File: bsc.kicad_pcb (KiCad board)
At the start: 2 copper layers, 120 x 72 mm, 155 parts, among them IC1 ILD217T, IC2 ILD217T, J1 AVR-ISP-6, J2 Prog, J3 U0TXD silent, J4 Boot, K1 TIANBO-HJR-4102-L, K2 TIANBO-HJR-4102-L, K3 TIANBO-HJR-4102-L, K4 TIANBO-HJR-4102-L, K5 TIANBO-HJR-4102-L, K6 TIANBO-HJR-4102-L, K7 TIANBO-HJR-4102-L, K8 AQY210S, Q1 BSS138, Q10 BC846, Q11 BC846, Q2 BSS138, Q3 BSS138, Q4 BSS138, Q5 BSS138, Q6 BSS138, Q7 BSS138, Q8 BC846, Q9 BC846, U1 LMO78_03-0.5, U10 74HC595, U11 74HC14, U12 74HC165, U2 ESP32WROOM32E16, U3 ATtiny24A-SS, U4 ADuM1201AR, U5 ADuM1201AR, U6 ADuM1201AR, U7 SN65HVD234, U8 SP3485EN, U9 SP3485EN, X1 Conn_S2, X2 Conn_S1, X3 Conn_DI, X4 Conn_SV, X5 Conn_Rel2, X6 Conn_Rel1

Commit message: Redesign PCB
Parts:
- removed J3: U0TXD silent, Connector_PinHeader_2.54mm:PinHeader_1x02_P2.54mm_Vertical
- removed K1: TIANBO-HJR-4102-L, Relay_THT:Relay_SPDT_HJR-4102
- removed K8: AQY210S, SamacSys_Parts:SOP254P962X275-4N
- removed R9: 180R, Resistor_SMD:R_0603_1608Metric
- removed U3: ATtiny24A-SS, Package_SO:SOIC-14_3.9x8.7mm_P1.27mm
- added C29: 22µ, Capacitor_SMD:CP_Elec_4x5.8, F.Cu at (115.6, 59.7)
- added C30: 100n, Capacitor_SMD:C_0603_1608Metric, F.Cu at (82.2, 49.7)
- added C31: 100n, Capacitor_SMD:C_0603_1608Metric, F.Cu at (107.4, 52.2)
- added C32: 100n, Capacitor_SMD:C_0603_1608Metric, F.Cu at (82.2, 42.2)
- added C33: 100n, Capacitor_SMD:C_0603_1608Metric, F.Cu at (107.4, 44.1)
- added C34: 22µ, Capacitor_SMD:CP_Elec_4x5.8, F.Cu at (85.1, 45.5)
- added C35: 22µ, Capacitor_SMD:CP_Elec_4x5.8, F.Cu at (109.5, 48.0)
- added C36: 100n, Capacitor_SMD:C_0603_1608Metric, B.Cu at (69.6, 49.0)
- added C37: 100n, Capacitor_SMD:C_0603_1608Metric, B.Cu at (94.9, 49.0)
- added C38: 100n, Capacitor_SMD:C_0603_1608Metric, F.Cu at (94.9, 49.7)
- added C39: 100n, Capacitor_SMD:C_0603_1608Metric, F.Cu at (94.9, 42.1)
- added C40: 100n, Capacitor_SMD:C_0603_1608Metric, F.Cu at (72.8, 50.2)
- added C41: 100n, Capacitor_SMD:C_0603_1608Metric, F.Cu at (84.8, 50.7)
- added C42: 22µ, Capacitor_SMD:CP_Elec_4x5.8, F.Cu at (97.8, 45.5)
- added C43: 100n, Capacitor_SMD:C_0603_1608Metric, F.Cu at (97.4, 49.9)
- added C44: 100n, Capacitor_SMD:C_0603_1608Metric, F.Cu at (74.0, 62.1)
- added C45: 100n, Capacitor_SMD:C_0603_1608Metric, B.Cu at (82.2, 49.0)
- added C46: 100n, Capacitor_SMD:C_0603_1608Metric, F.Cu at (88.1, 66.2)
- added C47: 100n, Capacitor_SMD:C_0603_1608Metric, F.Cu at (102.9, 63.5)
- added C48: 100n, Capacitor_SMD:C_0603_1608Metric, B.Cu at (42.5, 66.3)
- added C49: 100n, Capacitor_SMD:C_0603_1608Metric, F.Cu at (61.6, 78.0)
- added C50: 100µ, Capacitor_SMD:CP_Elec_6.3x5.9, F.Cu at (53.3, 87.7)
- added C51: 100n, Capacitor_SMD:C_0603_1608Metric, F.Cu at (65.5, 88.3)
- added C52: 100µ, Capacitor_SMD:CP_Elec_6.3x5.9, F.Cu at (52.6, 80.4)
- added C53: 100n, Capacitor_SMD:C_0603_1608Metric, F.Cu at (62.3, 88.4)
- added C54: 100n, Capacitor_SMD:C_0603_1608Metric, B.Cu at (41.0, 66.3)
- added C55: 100n, Capacitor_SMD:C_0603_1608Metric, B.Cu at (44.2, 66.3)
- added C60: 100n, Capacitor_SMD:C_0603_1608Metric, F.Cu at (73.0, 80.8)
- added D24: LL4148, Diode_SMD:D_MiniMELF, B.Cu at (72.1, 36.8)
- added F1: BELFUSE, Fuse:Fuse_0679H, F.Cu at (36.0, 89.1)
- added F2: BELFUSE, Fuse:Fuse_0679H, F.Cu at (44.1, 89.1)
- added H1: MountingHole, MountingHole:MountingHole_3.2mm_M3, F.Cu at (35.0, 21.0)
- added H2: MountingHole, MountingHole:MountingHole_3.2mm_M3, F.Cu at (145.0, 21.0)
- added H3: MountingHole, MountingHole:MountingHole_3.2mm_M3, F.Cu at (145.0, 111.0)
- added H4: MountingHole, MountingHole:MountingHole_3.2mm_M3, F.Cu at (35.0, 111.0)
- added IC3: ILD217T, Package_SO:SOIC-8_5.23x5.23mm_P1.27mm, F.Cu at (67.7, 58.4)
- added IC4: ILD217T, Package_SO:SOIC-8_5.23x5.23mm_P1.27mm, F.Cu at (88.6, 58.4)
- added J10: JP_REL1_COM_12V, Connector_PinHeader_2.54mm:PinHeader_1x02_P2.54mm_Vertical, F.Cu at (137.9, 89.2)
- added J11: Conn_Extension, Connector_PinHeader_2.54mm:PinHeader_2x05_P2.54mm_Vertical, F.Cu at (33.1, 74.5)
- added J12: JP_REL2_COM_12V, Connector_PinHeader_2.54mm:PinHeader_1x02_P2.54mm_Vertical, F.Cu at (125.2, 89.2)
- added J13: JP_REL3_COM_12V, Connector_PinHeader_2.54mm:PinHeader_1x02_P2.54mm_Vertical, F.Cu at (112.5, 89.2)
- added J14: Conn_REL1, Connector_PinHeader_2.54mm:PinHeader_1x03_P2.54mm_Vertical, F.Cu at (135.1, 75.7)
- added J15: Conn_REL2, Connector_PinHeader_2.54mm:PinHeader_1x03_P2.54mm_Vertical, F.Cu at (135.1, 85.1)
- added J16: Conn_REL3, Connector_PinHeader_2.54mm:PinHeader_1x03_P2.54mm_Vertical, F.Cu at (108.7, 80.5)
- added J5: JP_REL4_COM_12V, Connector_PinHeader_2.54mm:PinHeader_1x02_P2.54mm_Vertical, F.Cu at (99.8, 89.2)
- added J8: JP_REL5_COM_12V, Connector_PinHeader_2.54mm:PinHeader_1x02_P2.54mm_Vertical, F.Cu at (87.1, 89.2)
- added J9: JP_REL6_COM_12V, Connector_PinHeader_2.54mm:PinHeader_1x02_P2.54mm_Vertical, F.Cu at (74.4, 89.2)
- added JP10: JP_U1_TX_TXS, Jumper:SolderJumper-2_P1.3mm_Open_RoundedPad1.0x1.5mm, B.Cu at (71.1, 62.7)
- added JP11: JP_U1_RXS_RXO, Jumper:SolderJumper-2_P1.3mm_Open_RoundedPad1.0x1.5mm, B.Cu at (76.5, 54.5)
- added JP12: JP_U1_TXS_TXO, Jumper:SolderJumper-2_P1.3mm_Open_RoundedPad1.0x1.5mm, B.Cu at (68.6, 54.5)
- added JP13: JP_U1_TXEN_TXENS, Jumper:SolderJumper-2_P1.3mm_Open_RoundedPad1.0x1.5mm, F.Cu at (67.1, 57.1)
- added JP14: JP_U2_3V3_VCC, Jumper:SolderJumper-2_P1.3mm_Open_RoundedPad1.0x1.5mm, B.Cu at (93.0, 40.6)
- added JP15: JP_U2_GND_GNDS, Jumper:SolderJumper-2_P1.3mm_Open_RoundedPad1.0x1.5mm, B.Cu at (89.4, 51.3)
- added JP16: JP_U2_RX_RXS, Jumper:SolderJumper-2_P1.3mm_Open_RoundedPad1.0x1.5mm, B.Cu at (91.7, 62.7)
- added JP17: JP_U2_TX_TXS, Jumper:SolderJumper-2_P1.3mm_Open_RoundedPad1.0x1.5mm, B.Cu at (83.6, 62.7)
- added JP18: JP_U2_RXS_RXO, Jumper:SolderJumper-2_P1.3mm_Open_RoundedPad1.0x1.5mm, B.Cu at (88.9, 54.5)
- added JP19: JP_U2_TXS_TXO, Jumper:SolderJumper-2_P1.3mm_Open_RoundedPad1.0x1.5mm, B.Cu at (81.0, 54.5)
- added JP20: JP_U2_TXEN_TXENS, Jumper:SolderJumper-2_P1.3mm_Open_RoundedPad1.0x1.5mm, F.Cu at (67.1, 59.7)
- added JP21: JP_U3_3V3_VCC, Jumper:SolderJumper-2_P1.3mm_Open_RoundedPad1.0x1.5mm, B.Cu at (105.8, 40.6)
- added JP22: JP_U3_GND_GNDS, Jumper:SolderJumper-2_P1.3mm_Open_RoundedPad1.0x1.5mm, B.Cu at (102.1, 51.6)
- added JP23: JP_U3_RX_RXS, Jumper:SolderJumper-2_P1.3mm_Open_RoundedPad1.0x1.5mm, B.Cu at (101.2, 62.4)
- added JP24: JP_U3_TX_TXS, Jumper:SolderJumper-2_P1.3mm_Open_RoundedPad1.0x1.5mm, B.Cu at (98.7, 62.4)
- added JP25: JP_U3_RXS_RXO, Jumper:SolderJumper-2_P1.3mm_Open_RoundedPad1.0x1.5mm, B.Cu at (101.1, 54.7)
- added JP26: JP_U3_TXS_TXO, Jumper:SolderJumper-2_P1.3mm_Open_RoundedPad1.0x1.5mm, B.Cu at (93.2, 54.7)
- added JP27: JP_U3_TXEN_TXENS, Jumper:SolderJumper-2_P1.3mm_Open_RoundedPad1.0x1.5mm, F.Cu at (87.4, 57.7)
- added JP28: 12V_5V, Jumper:SolderJumper-2_P1.3mm_Open_RoundedPad1.0x1.5mm, B.Cu at (59.6, 82.3)
- added JP29: JP_REL_VCC, Jumper:SolderJumper-3_P1.3mm_Open_RoundedPad1.0x1.5mm, B.Cu at (56.5, 91.4)
- added JP30: JP_EXT_5V, Jumper:SolderJumper-2_P1.3mm_Open_RoundedPad1.0x1.5mm, B.Cu at (36.4, 87.4)
- added JP31: JP_EXT_3V3, Jumper:SolderJumper-2_P1.3mm_Open_RoundedPad1.0x1.5mm, B.Cu at (38.1, 81.5)
- added JP7: JP_U1_3V3_VCC, Jumper:SolderJumper-2_P1.3mm_Open_RoundedPad1.0x1.5mm, B.Cu at (80.4, 40.6)
- added JP8: JP_U1_GND_GNDS, Jumper:SolderJumper-2_P1.3mm_Open_RoundedPad1.0x1.5mm, B.Cu at (76.6, 51.3)
- added JP9: JP_U1_RX_RXS, Jumper:SolderJumper-2_P1.3mm_Open_RoundedPad1.0x1.5mm, B.Cu at (79.0, 62.7)
- added PS1: 1S4E_0503S1U, custom_th:Converter_DCDC_GAPTEC_1S4E_S1U, F.Cu at (66.9, 50.9)
- added PS2: TEA 1-0505, Converter_DCDC:Converter_DCDC_Murata_MEE1SxxxxSC_THT, F.Cu at (111.6, 65.6)
- added PS3: 1S4E_0503S1U, custom_th:Converter_DCDC_GAPTEC_1S4E_S1U, F.Cu at (79.4, 50.8)
- added PS4: 1S4E_0503S1U, custom_th:Converter_DCDC_GAPTEC_1S4E_S1U, F.Cu at (104.8, 50.8)
- added PS5: 1S4E_0503S1U, custom_th:Converter_DCDC_GAPTEC_1S4E_S1U, F.Cu at (92.1, 50.8)
- added Q12: IRLML2244, Package_TO_SOT_SMD:SOT-23, F.Cu at (45.5, 80.4)
- added Q13: BC857BS, Package_TO_SOT_SMD:SOT-363_SC-70-6, F.Cu at (41.5, 84.6)
- added Q14: IRLML2244, Package_TO_SOT_SMD:SOT-23, F.Cu at (45.5, 84.2)
- added R56: n.b., Resistor_SMD:R_0603_1608Metric, F.Cu at (120.8, 57.1)
- added R57: 330R, Resistor_SMD:R_0603_1608Metric, F.Cu at (63.8, 58.0)
- added R58: 330R, Resistor_SMD:R_0603_1608Metric, F.Cu at (63.8, 61.4)
- added R59: 330R, Resistor_SMD:R_0603_1608Metric, F.Cu at (84.6, 57.9)
- added R60: 2k2, Resistor_SMD:R_0603_1608Metric, F.Cu at (73.2, 58.4)
- added R61: 2k2, Resistor_SMD:R_0603_1608Metric, F.Cu at (95.9, 52.7)
- added R62: 2k2, Resistor_SMD:R_0603_1608Metric, F.Cu at (71.6, 54.0)
- added R63: n.b., Resistor_SMD:R_0603_1608Metric, B.Cu at (76.7, 40.4)
- added R64: n.b., Resistor_SMD:R_0603_1608Metric, B.Cu at (107.2, 44.5)
- added R65: n.b., Resistor_SMD:R_0603_1608Metric, B.Cu at (89.2, 40.3)
- added R66: 10k, Resistor_SMD:R_0603_1608Metric, F.Cu at (73.0, 77.3)
- added R67: 2k4, Resistor_SMD:R_0603_1608Metric, F.Cu at (72.1, 73.0)
- added R68: 470R, Resistor_SMD:R_0603_1608Metric, F.Cu at (72.1, 74.8)
- added R69: 47k, Resistor_SMD:R_0603_1608Metric, F.Cu at (64.5, 79.0)
- added R70: 20k, Resistor_SMD:R_0603_1608Metric, F.Cu at (67.8, 79.0)
- added R71: 10k, Resistor_SMD:R_0603_1608Metric, F.Cu at (71.2, 77.3)
- added R74: 4k7, Resistor_SMD:R_0603_1608Metric, F.Cu at (69.1, 90.1)
- added R75: 4k7, Resistor_SMD:R_0603_1608Metric, F.Cu at (69.0, 88.4)
- added R76: 4k7, Resistor_SMD:R_0603_1608Metric, F.Cu at (71.2, 86.0)
- added R77: 4k7, Resistor_SMD:R_0603_1608Metric, F.Cu at (72.9, 85.4)
- added R78: 4k7, Resistor_SMD:R_0603_1608Metric, F.Cu at (71.3, 81.4)
- added R79: 4k7, Resistor_SMD:R_0603_1608Metric, F.Cu at (71.5, 89.3)
- added U13: ADuM1201AR, Package_SO:SOIC-8_3.9x4.9mm_P1.27mm, B.Cu at (50.5, 43.9)
- added U14: NCP1117-3.3_SOT223, Package_TO_SOT_SMD:SOT-223-3_TabPin2, B.Cu at (74.4, 45.6)
- added U15: NCP1117-3.3_SOT223, Package_TO_SOT_SMD:SOT-223-3_TabPin2, B.Cu at (99.8, 45.7)
- added U16: SP3485EN, Package_SO:SOIC-8_3.9x4.9mm_P1.27mm, B.Cu at (85.0, 54.5)
- added U17: NCP1117-3.3_SOT223, Package_TO_SOT_SMD:SOT-223-3_TabPin2, B.Cu at (86.9, 45.6)
- added U18: TS912, Package_SO:SO-8_3.9x4.9mm_P1.27mm, F.Cu at (66.3, 75.4)
- added U19: LMO78_05-0.5, custom_th:Converter_DCDC_RECOM_R-78E-1.0, F.Cu at (64.4, 83.6)
- added U20: HC 151, Package_SO:SOIC-16_3.9x9.9mm_P1.27mm, B.Cu at (67.9, 79.3)
- added mouse-bite-3mm-slot: VAL**, mouse_bites:mouse-bite-3mm-slot, F.Cu at (142.5, 28.5)
- added mouse-bite-3mm-slot: VAL**, mouse_bites:mouse-bite-3mm-slot, F.Cu at (142.5, 103.5)
- added mouse-bite-3mm-slot: VAL**, mouse_bites:mouse-bite-3mm-slot, F.Cu at (37.5, 103.5)
- added mouse-bite-3mm-slot: VAL**, mouse_bites:mouse-bite-3mm-slot, F.Cu at (37.5, 28.5)
- added mouse-bite-3mm-slot: VAL**, mouse_bites:mouse-bite-3mm-slot, F.Cu at (90.0, 103.5)
- added mouse-bite-3mm-slot: VAL**, mouse_bites:mouse-bite-3mm-slot, F.Cu at (90.0, 28.5)
- C1: value 10µ -> 100µ
- C10, C11, C13, C14, C20, C22, C27, D10, D14, D15, D18, D19, D5, D6, D7, D8, D9, Q11, Q9, R2, R26, R28, R30, R32, R34, R36, R40, R44: moved to F.Cu
- C12: value 100n -> 22µ; footprint Capacitor_SMD:C_0603_1608Metric -> Capacitor_SMD:CP_Elec_4x5.8; moved to F.Cu
- C15, C16, C5, C8: value 100nF -> 100n
- C4: value 22µ -> 470µ/6,3V; footprint Capacitor_SMD:CP_Elec_6.3x5.9 -> Capacitor_SMD:CP_Elec_8x10
- C6: value 22µ -> 100µ
- D2: value LED3 -> LL4148; footprint LED_SMD:LED_PLCC-2 -> Diode_SMD:D_MiniMELF; moved to B.Cu
- D20, D22: footprint Package_TO_SOT_SMD:SOT-323_SC-70 -> Package_TO_SOT_SMD:SOT-23
- D21, D23: footprint Package_TO_SOT_SMD:SOT-323_SC-70 -> Package_TO_SOT_SMD:SOT-23; moved to F.Cu
- J1: value AVR-ISP-6 -> Conn_JTAG_ESP; footprint Connector_PinHeader_2.54mm:PinHeader_2x03_P2.54mm_Vertical -> Connector_PinHeader_1.27mm:PinHeader_2x10_P1.27mm_Vertical_SMD; moved to B.Cu
- JP1: value O_U2RXD -> CAN_VCC
- JP2: value O_U2TXD -> CAN_GND
- JP3: value O_SU1RXD -> CAN_RC
- JP4: value O_SU1TXD -> CAN_TX
- JP5: value O_SU2RXD -> DI_VCC; moved to F.Cu
- JP6: value O_SU2TXD -> DI_GND; moved to F.Cu
- Q1: value BSS138 -> BC857BS; footprint Package_TO_SOT_SMD:SOT-23 -> Package_TO_SOT_SMD:SOT-363_SC-70-6
- Q5, Q6, Q7: value BSS138 -> IRLML 2502
- R19: value 180R -> n.b.; moved to B.Cu
- R37, R39, R41, R43, U12: moved to B.Cu
- R53, R54: value 10k -> n.b.
- R8: value 100k -> 10k
- U1: footprint Converter_DCDC:Converter_DCDC_RECOM_R-78E-0.5_THT -> custom_th:Converter_DCDC_RECOM_R-78E-1.0
- moved R7 68.4 mm to (38.8, 83.1), turned to 90 degrees
- moved R6 66.0 mm to (41.3, 76.7), turned to 180 degrees
- moved R5 56.7 mm to (38.8, 78.3), turned to 90 degrees
- moved JP3 55.1 mm to (50.7, 45.0), turned to 0 degrees
- moved JP4 46.7 mm to (50.7, 43.0), turned to 0 degrees
- moved C9 46.6 mm to (46.4, 45.2), turned to 180 degrees
- moved D3 40.3 mm to (58.2, 41.1)
- moved C8 39.9 mm to (65.1, 71.9), turned to 0 degrees
- moved J1 39.0 mm to (47.8, 60.1), turned to -90 degrees
- moved U4 35.1 mm to (75.1, 62.4)
- moved C1 35.0 mm to (76.8, 66.9), turned to 90 degrees
- moved C18 33.9 mm to (102.0, 69.1), turned to 0 degrees
- moved JP6 33.7 mm to (108.5, 64.1)
- moved C7 33.4 mm to (68.9, 71.9), turned to 180 degrees
- moved U1 32.8 mm to (66.9, 67.1), turned to 0 degrees
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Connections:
- net /INPUT/IO_DATA_IN_DS renamed /INPUT/IO_DATA_OUT
- net /OUTPUT/DATA_OUT renamed /OUTPUT/IO_DATA_IN
- C10 pad 1: +3V3 -> +5V
- C11 pad 1: +3V3 -> /CAN_VCC
- C11 pad 2: GND -> /CAN_GND
- C12 pad 1: +3V3 -> /CAN_VCC
- C12 pad 2: GND -> /CAN_GND
- C13 pad 1: +3V3 -> +5V
- C14 pad 1: +3V3 -> /INPUT/5V_1
- C14 pad 2: GND -> GND1
- C15 pad 2: GND -> /CAN_GND
- C16 pad 1: +3V3 -> /CAN_VCC
- C16 pad 2: GND -> /CAN_GND
- C7 pad 1: +3V3 -> +5V
- C8 pad 1: GND -> +3V3
- C8 pad 2: Net-(C8-Pad2) -> GND
- C9 pad 1: /AVR_RST -> +3V3
- D1 pad 1: GND -> Net-(D1-Pad1)
- D1 pad 2: Net-(D1-Pad2) -> +3V3
- D10 pad 1: +5V -> /OUTPUT/VCC_REL
- D2 pad 1: GND -> Net-(C37-Pad1)
- D2 pad 2: Net-(D2-Pad2) -> /serial/U3_VCC_e
- D3 pad 1: +5V -> Net-(C36-Pad1)
- D3 pad 2: Net-(D3-Pad2) -> /U1_VCC_e
- D4 pad 3: GND -> /CAN_GND
- D5 pad 1: +5V -> /OUTPUT/VCC_REL
- D6 pad 1: +5V -> /OUTPUT/VCC_REL
- D7 pad 1: +5V -> /OUTPUT/VCC_REL
- D8 pad 1: +5V -> /OUTPUT/VCC_REL
- D9 pad 1: +5V -> /OUTPUT/VCC_REL
- J1 pad 1: /AVR_MISO -> unconnected-(J1-Pad1)
- J1 pad 2: +3V3 -> unconnected-(J1-Pad2)
- J1 pad 3: /AVR_SCK -> /RST_ESP
- J1 pad 4: /AVR_MOSI -> GND
- J1 pad 5: /AVR_RST -> /H_MISO
- J4 pad 1: Net-(J4-Pad1) -> /LED1
- JP1 pad 1: /U1RX -> +3V3
- JP1 pad 2: /U1RX_O -> /CAN_VCC
- JP2 pad 1: /U1TX -> GND
- JP2 pad 2: /U1TX_O -> /CAN_GND
- JP3 pad 1: /U3RX -> /CAN_Rx
- JP3 pad 2: /U3RX_O -> /CAN_Rx_s
- JP4 pad 1: /U3TX -> /CAN_Tx
- JP4 pad 2: /U3TX_O -> /CAN_Tx_s
- JP5 pad 1: /U2RX -> +5V
- JP5 pad 2: /U2RX_O -> /INPUT/5V_1
- JP6 pad 1: /U2TX -> GND
- JP6 pad 2: /U2TX_O -> GND1
- K2 pad 5: +5V -> /OUTPUT/VCC_REL
- K3 pad 5: +5V -> /OUTPUT/VCC_REL
- K4 pad 5: +5V -> /OUTPUT/VCC_REL
- K5 pad 5: +5V -> /OUTPUT/VCC_REL
- K6 pad 5: +5V -> /OUTPUT/VCC_REL
- K7 pad 5: +5V -> /OUTPUT/VCC_REL
- Q1 pad 1: Net-(Q1-Pad1) -> Net-(F1-Pad2)
- Q1 pad 2: GND -> Net-(Q1-Pad2)
- Q1 pad 3: Net-(D3-Pad2) -> Net-(Q1-Pad3)
- R1 pad 1: +3V3 -> /RST_ESP
- R1 pad 2: /RST_ESP -> +3V3
- R10 pad 1: Net-(D1-Pad2) -> Net-(D1-Pad1)
- R10 pad 2: Net-(R10-Pad2) -> GND
- R11 pad 1: +3V3 -> /CAN_VCC
- R12 pad 1: GND -> /CAN_GND
- R19 pad 1: Net-(K8-Pad1) -> /CAN_GND
- R19 pad 2: /OUTPUT/DO1 -> /CAN_VCC
- R2 pad 1: +3V3 -> /onewire
- R2 pad 2: /onewire -> +3V3
- R24 pad 2: Net-(R24-Pad2) -> /LED1
- R5 pad 1: +3V3 -> Net-(Q1-Pad2)
- R5 pad 2: /AVR_RST -> GND
- R6 pad 1: GND -> Net-(Q1-Pad3)
- R6 pad 2: Net-(R6-Pad2) -> GND
- R7 pad 1: Net-(R6-Pad2) -> Net-(Q13-Pad2)
- R7 pad 2: Net-(R7-Pad2) -> GND
- R8 pad 1: Net-(Q1-Pad1) -> Net-(Q13-Pad3)
- U10 pad 6: /OUTPUT/DO1 -> /OUTPUT/T_ADDR0
- U10 pad 7: Net-(R24-Pad2) -> /OUTPUT/T_ADDR1
- U12 pad 4: GND -> +3V3
- U2 pad 12: Net-(J11-Pad9) -> /TACHO
- U2 pad 23: Net-(J3-Pad2) -> /T_ADDR2
- U2 pad 24: /WDT_TRIG_ESP_OUT -> /U2RXTX_EN
- U2 pad 25: Net-(J4-Pad1) -> /LED1
- U2 pad 6: /WDT_TRIG__ESP_IN -> /AI1d
- U4 pad 6: /U1TX_O -> /serial/U1TX_S
- U4 pad 7: /U1RX_O -> /serial/U1RX_S
- U4 pad 8: /U1_VCC -> /serial/U1_VCC
- U5 pad 5: /U3_GND -> /serial/U3_GND
- U5 pad 6: /U3TX_O -> /serial/U3TX_S
- U5 pad 7: /U3RX_O -> /serial/U3RX_S
- U5 pad 8: /U3_VCC -> /serial/U3_VCC
- U6 pad 5: /U2_GND -> /serial/U2_GND
- U6 pad 6: /U2TX_O -> /serial/U2TX_S
- U6 pad 7: /U2RX_O -> /serial/U2RX_S
- U6 pad 8: /U2_VCC -> /serial/U2_VCC
- U7 pad 1: /CAN_Tx -> /CAN_Tx_s
- U7 pad 2: GND -> /CAN_GND
- U7 pad 3: +3V3 -> /CAN_VCC
- U7 pad 4: /CAN_Rx -> /CAN_Rx_s
- U8 pad 1: /U1RX -> /serial/U1RX_S
- U8 pad 2: /U1RXTX_EN -> /serial/U1RXTX_ENs
- U8 pad 3: /U1RXTX_EN -> /serial/U1RXTX_ENs
- U8 pad 4: /U1TX -> /serial/U1TX_S
- U8 pad 5: GND -> /U1_GND
- U8 pad 8: +3V3 -> /serial/U1_VCC
- U9 pad 1: /U3RX -> /serial/U3RX_S
- U9 pad 2: /U3RXTX_EN -> /serial/U3RXTX_ENs
- U9 pad 3: /U3RXTX_EN -> /serial/U3RXTX_ENs
- U9 pad 4: /U3TX -> /serial/U3TX_S
- U9 pad 5: GND -> /serial/U3_GND
- U9 pad 6: /U3RX_O -> /serial/U3RX_O
- U9 pad 7: /U3TX_O -> /serial/U3TX_O
- U9 pad 8: +3V3 -> /serial/U3_VCC
- X1 pad 1: /U1_VCC -> GND
- X1 pad 2: /U1_GND -> +3V3
- X1 pad 3: /U1TX_O -> /onewire
- X1 pad 4: /U1RX_O -> /CAN_H
- X1 pad 5: /CAN_H -> /CAN_L
- X1 pad 6: /CAN_L -> /U1_VCC_e
- X1 pad 7: /onewire -> /U1_GND
- X1 pad 8: /SCL -> /U1TX_O
- X1 pad 9: /SDA -> /U1RX_O
- X2 pad 1: GND -> /serial/U2_VCC_e
- X2 pad 2: /U2_VCC -> /serial/U2_GND
- X2 pad 3: /U2_GND -> /serial/U2TX_O
- X2 pad 4: /U2TX_O -> /serial/U2RX_O
- X2 pad 5: /U2RX_O -> /serial/U3_VCC_e
- X2 pad 6: /U3_VCC -> /serial/U3_GND
- X2 pad 7: /U3_GND -> /serial/U3TX_O
- X2 pad 8: /U3TX_O -> /serial/U3RX_O
- X2 pad 9: /U3RX_O -> GND
- X3 pad 2: /INPUT/DI2_P -> /INPUT/5V_1
- X3 pad 3: /INPUT/DI3_P -> /INPUT/DI2_P
- X3 pad 4: /INPUT/DI4_P -> /INPUT/5V_1
- X3 pad 5: +5V -> /INPUT/DI3_P
- X3 pad 6: +5V -> /INPUT/5V_1
- X3 pad 7: GND1 -> /INPUT/DI4_P
- X3 pad 8: GND -> /INPUT/5V_1
- X3 pad 9: GND -> GND1
- X4 pad 1: /REL0_NO -> /AI1
- X4 pad 2: /REL0_NC -> V_IN
- X4 pad 3: /REL0_COM -> +5V
- X4 pad 8: GND -> V_IN2
- X4 pad 9: +5V -> V_IN1
- X5 pad 3: /OUTPUT/REL5_COM -> /OUTPUT/TACHO4
- X5 pad 4: /OUTPUT/REL5_NO -> /OUTPUT/REL5_COM
- X5 pad 5: /OUTPUT/REL6_COM -> /OUTPUT/REL5_NO
- X5 pad 6: /OUTPUT/REL6_NO -> /OUTPUT/TACHO5
- X5 pad 7: /OUTPUT/DO1_1 -> /OUTPUT/REL6_COM
- X5 pad 8: /OUTPUT/DO1_2 -> /OUTPUT/REL6_NO
- X5 pad 9: GND -> /OUTPUT/TACHO6
- X6 pad 2: /OUTPUT/REL1_NC -> /OUTPUT/REL1_NO
- X6 pad 3: /OUTPUT/REL1_NO -> /OUTPUT/REL1_NC_TACHO
- X6 pad 5: /OUTPUT/REL2_NC -> /OUTPUT/REL2_NO
- X6 pad 6: /OUTPUT/REL2_NO -> /OUTPUT/REL2_NC_TACHO
- X6 pad 8: /OUTPUT/REL3_NC -> /OUTPUT/REL3_NO
- X6 pad 9: /OUTPUT/REL3_NO -> /OUTPUT/REL3_NC_TACHO
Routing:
- net /OUTPUT/VCC_REL: track 0.00 -> 207.6 mm, vias 0 -> 1
- net V_IN: track 0.00 -> 170.5 mm, vias 0 -> 5
- net GND: track 617.5 -> 477.9 mm, vias 151 -> 194
- net +3V3: track 307.1 -> 444.3 mm, vias 8 -> 19
- net /WDT_TRIG_ESP_OUT: track 95.5 -> 0.00 mm, vias 2 -> 0
- net /serial/U2_GND: track 0.00 -> 84.7 mm, vias 0 -> 1
- net /OUTPUT/TACHO1: track 0.00 -> 79.2 mm, vias 0 -> 2
- net /OUTPUT/TACHO2: track 0.00 -> 73.7 mm, vias 0 -> 1
- net /U1_GND: track 8.38 -> 81.2 mm, vias 0 -> 3
- net /INPUT/5V_1: track 0.00 -> 68.0 mm
- net /serial/U3_GND: track 0.00 -> 67.1 mm, vias 0 -> 2
- net /WDT_TRIG__ESP_IN: track 60.0 -> 0.00 mm, vias 2 -> 0
- net /serial/U2_VCC: track 0.00 -> 60.0 mm, vias 0 -> 1
- net /T_ADDR2: track 0.00 -> 57.9 mm, vias 0 -> 3
- net /serial/U3_VCC: track 0.00 -> 57.1 mm, vias 0 -> 3
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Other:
- board size 120 x 72 mm -> 120 x 100 mm
- board text added: "(Frontside) JP5: +5V -> DI_VCC JP6: GND -> DI_GND"
- board text added: "1: Analogeingang 2: +5/+12V (je nach Bestückung) 3: +5V 4: +3V3"
- board text added: "1: DI 1 2: DI +5V 3: DI 2 4: DI +5V"
- board text added: "1: GND 2: +3V3 3: Onewire 4: CAN H 5: CAN L"
- board text added: "1: Rel 1 (COM) 2: Rel 1 (NO) 3: Rel 1 (NC)/Tacho 1"
- board text added: "1: Rel 4 (COM) 2: Rel 4 (NO) 3: Tacho 4"
- board text added: "1: U2 VCC 2: U2 GND 3: U2 TX 4: U2 RX"
- board text added: "4: Rel 2 (COM) 5: Rel 2 (NO) 6: Rel 2 (NC)/Tacho 2 7: Rel 3 (COM) 8: Rel 3 (NO) 9: Rel 2 (NC)/Tacho 3"
- board text added: "4: Rel 5 (COM) 5: Rel 5 (NO) 6: Tacho 5 7: Rel 6 (COM) 8: Rel 6 (NO) 9: Tacho 6"
- board text added: "5: DI 3 6: DI +5V 7: DI 4 8: DI +5V 9: DI GND"
- board text added: "5: GND 6: GND 7: GND 8: V IN2 9: V IN1"
- board text added: "5: U3 VCC 6: U3 GND 7: U3 TX 8: U3 RX 9: GND"
- board text added: "6: U1 VCC 7: U1 GND 8: U1 TX 9: U1 RX"
- board text added: "Battery safety controller V2.0 github.com/shining-man/bsc_fw created by T. Himmler 2022"
- board text added: "JP1: CAN VCC JP2: CAN GND JP3: CAN RX JP4: CAN TX"
- board text added: "JP28: V_IN -> +5V"
- board text added: "JP29 VCC REL: 1-2: +5V | 2-3: V_IN"
- board text added: "JP30: 5V to Ext.-Port JP31: 3V3 to Ext.-Port"
- board text added: "U1|U2|U3| JP 07|14|21|3V3->Ux_VCC JP 08|15|22|GND->Ux_GND JP 09|16|23|UxRX->UxRX_S JP 10|17|24|UxTX->UxTX_S JP 11|18|25|UxRX_S->UxRX_O JP 12|19|26|UxTX_S->UxTX_O JP 13|20|27|UxRXTX_EN->UxRXTX_ENs"
- board text removed: "Battery safety controller (BSC) V1.0 (c) T. Himmler 2022"
- board text removed: "JP1: Serial 1, RXD JP2: Serial 1, TXD JP3: Serial 2, RXD JP4: Serial 2, TXD JP5: Serial 3, RXD JP6: Serial 3, TXD"

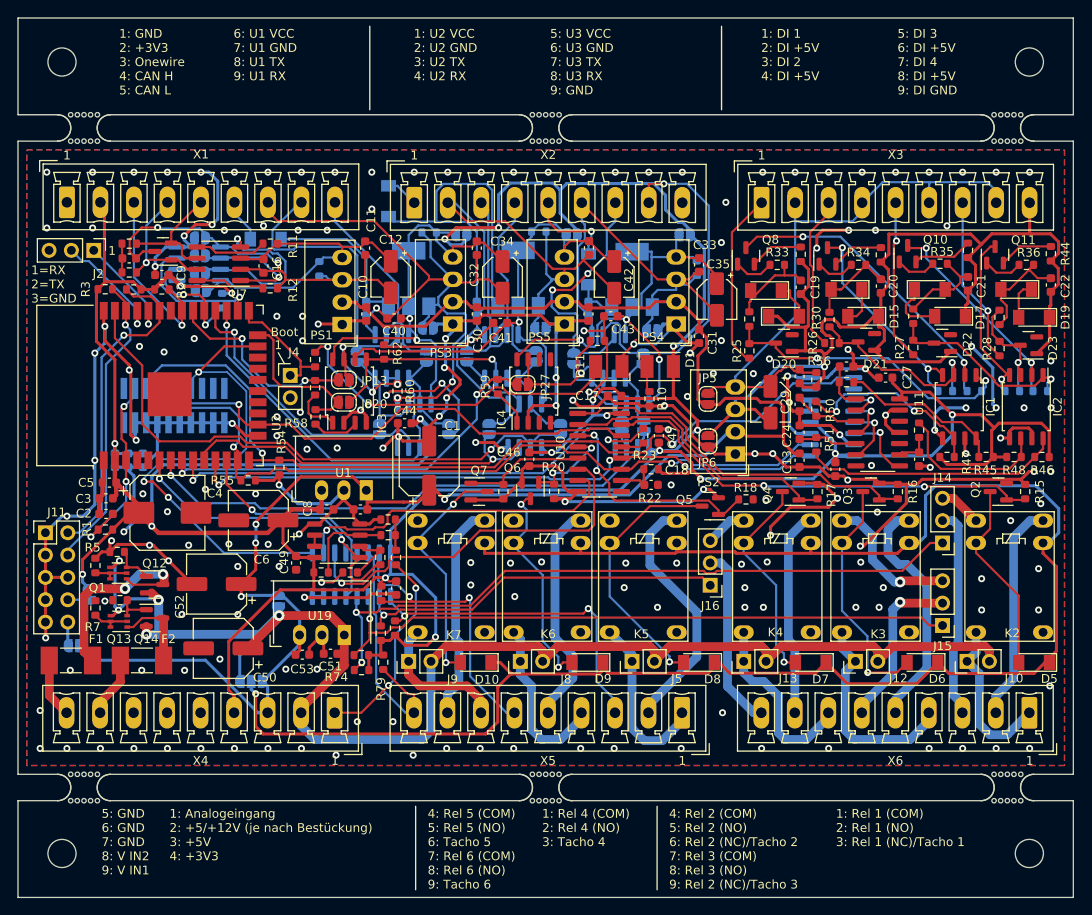
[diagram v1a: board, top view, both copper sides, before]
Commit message: Layout optimized
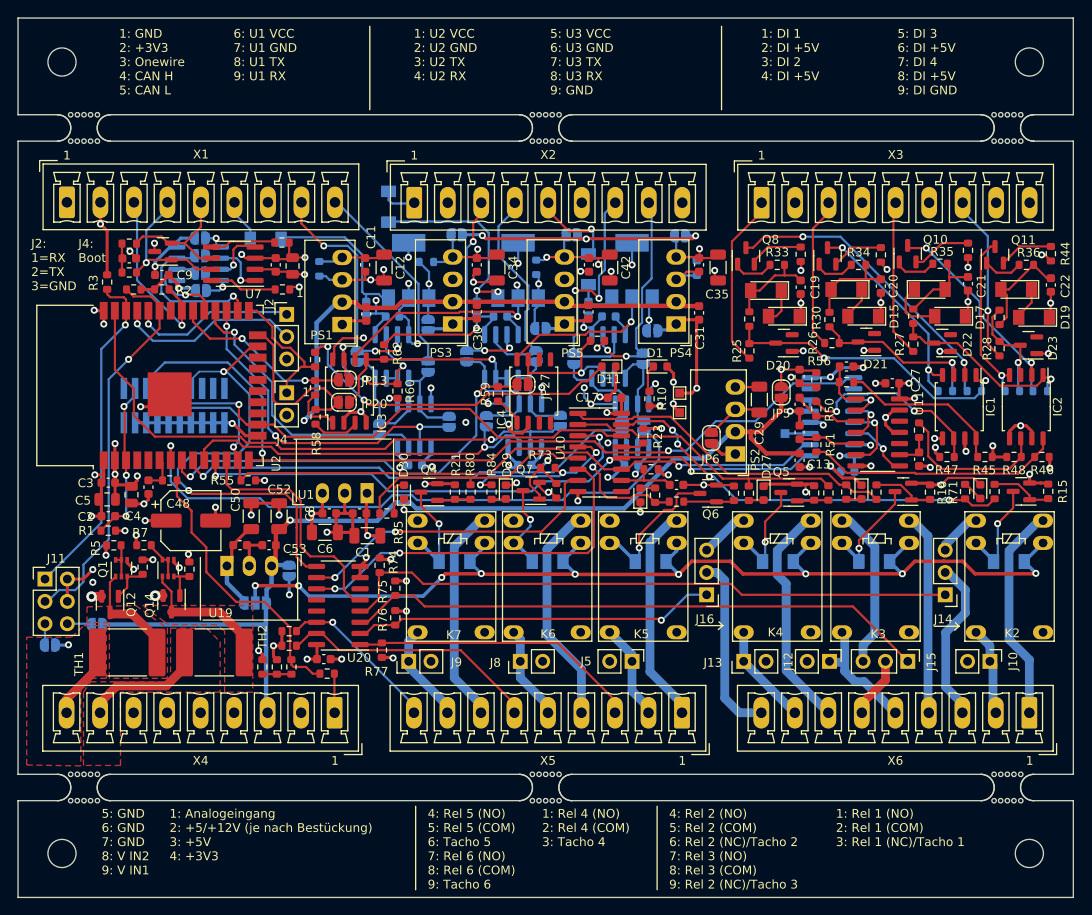
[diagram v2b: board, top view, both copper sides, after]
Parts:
- removed C55: 100n, Capacitor_SMD:C_0603_1608Metric
- removed F1, F2: BELFUSE, Fuse:Fuse_0679H
- removed U18: TS912, Package_SO:SO-8_3.9x4.9mm_P1.27mm
- added D25: LED_REL1, LED_SMD:LED_0603_1608Metric, F.Cu at (139.4, 69.8)
- added D26: LED_REL2, LED_SMD:LED_0603_1608Metric, F.Cu at (125.9, 69.9)
- added D27: LED_REL3, LED_SMD:LED_0603_1608Metric, F.Cu at (114.8, 70.0)
- added D28: LED_REL4, LED_SMD:LED_0603_1608Metric, F.Cu at (100.8, 70.3)
- added D29: LED_REL5, LED_SMD:LED_0603_1608Metric, F.Cu at (85.5, 69.9)
- added D30: LED_REL6, LED_SMD:LED_0603_1608Metric, F.Cu at (73.9, 69.9)
- added R72: 20, Resistor_SMD:R_0603_1608Metric, F.Cu at (104.9, 71.0)
- added R73: 20, Resistor_SMD:R_0603_1608Metric, F.Cu at (90.2, 67.2)
- added R80: 20, Resistor_SMD:R_0603_1608Metric, F.Cu at (81.5, 69.9)
- added R81: 270R, Resistor_SMD:R_0603_1608Metric, F.Cu at (124.2, 69.9)
- added R82: 270R, Resistor_SMD:R_0603_1608Metric, F.Cu at (113.1, 70.0)
- added R83: 270R, Resistor_SMD:R_0603_1608Metric, F.Cu at (102.4, 70.3)
- added R84: 270R, Resistor_SMD:R_0603_1608Metric, F.Cu at (83.8, 69.9)
- added R85: 270R, Resistor_SMD:R_0603_1608Metric, F.Cu at (71.9, 72.3)
- added R9: 20, Resistor_SMD:R_0603_1608Metric, F.Cu at (141.0, 69.8)
- added TH1: PTC FSMD2002920, Fuse:Fuse_2920_7451Metric, F.Cu at (42.4, 88.1)
- added TH2: PTC FSMD2002920, Fuse:Fuse_2920_7451Metric, F.Cu at (52.3, 88.1)
- added TP1: TP_GND, TestPoint:TestPoint_Pad_1.0x1.0mm, F.Cu at (105.2, 58.6)
- added TP3: TP_3V3, TestPoint:TestPoint_Pad_1.0x1.0mm, F.Cu at (105.2, 60.9)
- added TP5: TP, TestPoint:TestPoint_Pad_1.0x1.0mm, B.Cu at (117.2, 63.2)
- C1, C50: value 100µ -> 10µ/50V; footprint Capacitor_SMD:CP_Elec_6.3x5.9 -> Capacitor_SMD:C_1206_3216Metric
- C12, C29, C34, C35, C42: value 22µ -> 22µ/10V; footprint Capacitor_SMD:CP_Elec_4x5.8 -> Capacitor_SMD:C_1206_3216Metric
- C28, C40, C41, C43, C44, C46, C47, D10, D5, D6, D7, D8, D9: moved to B.Cu
- C4: value 470µ/6,3V -> 22µ/10V; footprint Capacitor_SMD:CP_Elec_8x10 -> Capacitor_SMD:C_0805_2012Metric
- C48: value 100n -> 100µ; footprint Capacitor_SMD:C_0603_1608Metric -> Capacitor_SMD:CP_Elec_6.3x5.9; moved to F.Cu
- C49: value 100n -> 10n
- C5: value 100n -> 4u7/25V; footprint Capacitor_SMD:C_0603_1608Metric -> Capacitor_SMD:C_0805_2012Metric
- C52, C6: value 100µ -> 22µ/10V; footprint Capacitor_SMD:CP_Elec_6.3x5.9 -> Capacitor_SMD:C_1206_3216Metric
- C54: value 100n -> 10µ; footprint Capacitor_SMD:C_0603_1608Metric -> Capacitor_SMD:C_0805_2012Metric; moved to F.Cu
- D1, D11: footprint LED_SMD:LED_PLCC-2 -> LED_SMD:LED_0603_1608Metric
- J11: footprint Connector_PinHeader_2.54mm:PinHeader_2x05_P2.54mm_Vertical -> Connector_PinHeader_2.54mm:PinHeader_2x03_P2.54mm_Vertical
- Q5, Q6, Q7: value IRLML 2502 -> BSS138
- R10, R24: value 180R -> 270R
- R15, R16, R17, R18, R20, R21: value 100k -> 10k
- R53: value n.b. -> 20; moved to F.Cu
- R54: value n.b. -> 20
- R66: value 10k -> 1k
- R67: value 2k4 -> 8k2
- R68: value 470R -> 2k4
- R69: value 47k -> 300R
- R70: value 20k -> 3k3
- R71: value 10k -> 270R
- U20: moved to F.Cu
- moved R53 77.5 mm to (127.6, 69.9)
- moved R71 66.9 mm to (137.7, 69.8)
- moved R54 62.5 mm to (122.1, 70.0)
- moved Q4 41.1 mm to (76.8, 69.9)
- moved C54 29.9 mm to (61.2, 44.2)
- moved R66 27.2 mm to (47.2, 68.6), turned to 0 degrees
- moved J2 23.1 mm to (60.6, 49.7), turned to 0 degrees
- moved Q6 20.2 mm to (108.5, 70.1), turned to 180 degrees
- moved C49 18.9 mm to (44.8, 69.3)
- moved R67 18.8 mm to (65.2, 90.6)
- moved R68 18.6 mm to (61.1, 89.8), turned to -90 degrees
- moved C51 16.1 mm to (55.2, 75.9), turned to 0 degrees
- moved C50 15.4 mm to (56.5, 72.6), turned to 90 degrees
- moved R70 13.6 mm to (59.4, 89.8), turned to 90 degrees
- moved C53 13.0 mm to (58.5, 75.9), turned to 180 degrees
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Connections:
- C1 pad 1: +5V -> V_IN
- C4 pad 1: +3V3 -> GND
- C4 pad 2: GND -> +3V3
- C44 pad 1: +3V3 -> GND
- C44 pad 2: GND -> +3V3
- C46 pad 1: +3V3 -> GND
- C46 pad 2: GND -> +3V3
- C47 pad 1: +3V3 -> GND
- C47 pad 2: GND -> +3V3
- C49 pad 1: +3V3 -> /AI1d
- C5 pad 1: +3V3 -> GND
- C5 pad 2: GND -> +3V3
- C54 pad 1: +3V3 -> /CAN_VCC
- C54 pad 2: GND -> /CAN_GND
- C7 pad 1: +5V -> V_IN
- C9 pad 1: +3V3 -> GND
- C9 pad 2: GND -> +3V3
- J11 pad 1: GND -> /SCL
- J11 pad 2: /SDA -> GND
- J11 pad 3: GND -> /SDA
- J11 pad 4: /SCL -> GND
- J11 pad 5: GND -> Net-(J11-Pad5)
- J11 pad 6: GND -> Net-(J11-Pad6)
- JP30 pad 2: Net-(J11-Pad10) -> Net-(J11-Pad6)
- JP31 pad 2: Net-(J11-Pad8) -> Net-(J11-Pad5)
- Q2 pad 1: /OUTPUT/REL1 -> Net-(Q2-Pad1)
- Q3 pad 1: /OUTPUT/REL2 -> Net-(Q3-Pad1)
- Q4 pad 1: /OUTPUT/REL3 -> Net-(Q4-Pad1)
- Q4 pad 3: Net-(D7-Pad2) -> Net-(D10-Pad2)
- Q5 pad 1: /OUTPUT/REL4 -> Net-(Q5-Pad1)
- Q5 pad 3: Net-(D8-Pad2) -> Net-(D7-Pad2)
- Q6 pad 1: /OUTPUT/REL5 -> Net-(Q6-Pad1)
- Q6 pad 3: Net-(D9-Pad2) -> Net-(D8-Pad2)
- Q7 pad 1: /OUTPUT/REL6 -> Net-(Q7-Pad1)
- Q7 pad 3: Net-(D10-Pad2) -> Net-(D9-Pad2)
- R15 pad 1: /OUTPUT/REL1 -> Net-(Q2-Pad1)
- R16 pad 1: /OUTPUT/REL2 -> Net-(Q3-Pad1)
- R17 pad 1: /OUTPUT/REL3 -> Net-(Q5-Pad1)
- R18 pad 1: /OUTPUT/REL4 -> Net-(Q6-Pad1)
- R20 pad 1: /OUTPUT/REL5 -> Net-(Q7-Pad1)
- R21 pad 1: /OUTPUT/REL6 -> Net-(Q4-Pad1)
- R53 pad 1: +3V3 -> Net-(Q3-Pad1)
- R53 pad 2: /CAN_Rx -> /OUTPUT/REL2
- R54 pad 1: GND -> Net-(Q5-Pad1)
- R54 pad 2: /H_MISO -> /OUTPUT/REL3
- R66 pad 1: /AI1 -> /AI1d
- R67 pad 1: Net-(R66-Pad2) -> /AI1
- R67 pad 2: GND -> Net-(R66-Pad2)
- R68 pad 1: Net-(R68-Pad1) -> Net-(R66-Pad2)
- R68 pad 2: Net-(R66-Pad2) -> Net-(R68-Pad2)
- R69 pad 1: +3V3 -> Net-(R68-Pad2)
- R69 pad 2: Net-(R68-Pad1) -> GND
- R70 pad 1: Net-(R70-Pad1) -> Net-(R68-Pad2)
- R70 pad 2: GND -> +3V3
- R71 pad 1: /AI1d -> /OUTPUT/REL1
- R71 pad 2: Net-(R70-Pad1) -> Net-(D25-Pad2)
- U1 pad 1: +5V -> V_IN
- U12 pad 3: GND -> Net-(TP5-Pad1)
- X5 pad 1: /OUTPUT/REL4_COM -> /OUTPUT/REL4_NO
- X5 pad 2: /OUTPUT/REL4_NO -> /OUTPUT/REL4_COM
- X5 pad 4: /OUTPUT/REL5_COM -> /OUTPUT/REL5_NO
- X5 pad 5: /OUTPUT/REL5_NO -> /OUTPUT/REL5_COM
- X5 pad 7: /OUTPUT/REL6_COM -> /OUTPUT/REL6_NO
- X5 pad 8: /OUTPUT/REL6_NO -> /OUTPUT/REL6_COM
- X6 pad 1: /OUTPUT/REL1_COM -> /OUTPUT/REL1_NO
- X6 pad 2: /OUTPUT/REL1_NO -> /OUTPUT/REL1_COM
- X6 pad 4: /OUTPUT/REL2_COM -> /OUTPUT/REL2_NO
- X6 pad 5: /OUTPUT/REL2_NO -> /OUTPUT/REL2_COM
- X6 pad 7: /OUTPUT/REL3_COM -> /OUTPUT/REL3_NO
- X6 pad 8: /OUTPUT/REL3_NO -> /OUTPUT/REL3_COM
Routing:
- net +3V3: track 444.3 -> 167.8 mm, vias 19 -> 33
- net GND: track 477.9 -> 321.6 mm, vias 194 -> 55
- net GND1: track 135.0 -> 31.3 mm, vias 1 -> 13
- net /OUTPUT/VCC_REL: track 207.6 -> 124.0 mm, vias 1 -> 9
- net /INPUT/5V_1: track 68.0 -> 8.96 mm, vias 0 -> 1
- net /serial/U2_GND: track 84.7 -> 46.3 mm, vias 1 -> 5
- net /U1_GND: track 81.2 -> 44.7 mm, vias 3 -> 4
- net /AI1d: track 35.8 -> 4.02 mm, vias 2 -> 0
- net /serial/U3_GND: track 67.1 -> 35.6 mm, vias 2 -> 6
- net Net-(R66-Pad2): track 3.52 -> 31.9 mm
- net /CAN_GND: track 50.8 -> 26.1 mm, vias 2 -> 7
- net /serial/U1_VCC: track 52.5 -> 28.9 mm, vias 2 -> 6
- net Net-(C45-Pad1): track 42.6 -> 22.8 mm, vias 0 -> 2
- net /serial/U3_VCC: track 57.1 -> 38.1 mm, vias 3 -> 4
- net /AI1: track 23.4 -> 4.46 mm, vias 2 -> 0
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- added copper zone on In2.Cu, net +3V3
- added copper zone on In1.Cu, net /CAN_GND
- added copper zone on In2.Cu, net /CAN_VCC
- added copper zone on In2.Cu, net /INPUT/5V_1
- added copper zone on In1.Cu, net /U1_GND
- added copper zone on In2.Cu, net /serial/U1_VCC
- added copper zone on In1.Cu, net /serial/U2_GND
- added copper zone on In2.Cu, net /serial/U2_VCC
- added copper zone on In1.Cu, net /serial/U3_GND
- added copper zone on In2.Cu, net /serial/U3_VCC
- added copper zone on In1.Cu, net GND
- added copper zone on In1.Cu, net GND1
- added copper zone on F.Cu, net Net-(Q1-Pad1)
- added copper zone on F.Cu, net Net-(Q13-Pad1)
- added copper zone on F.Cu, net V_IN1
- added copper zone on F.Cu, net V_IN2
- removed copper zone on B.Cu, net GND
- removed copper zone on F.Cu, net GND
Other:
- copper layers 2 -> 4
- board text added: "1: Rel 1 (NO) 2: Rel 1 (COM) 3: Rel 1 (NC)/Tacho 1"
- board text added: "1: Rel 4 (NO) 2: Rel 4 (COM) 3: Tacho 4"
- board text added: "4: Rel 2 (NO) 5: Rel 2 (COM) 6: Rel 2 (NC)/Tacho 2 7: Rel 3 (NO) 8: Rel 3 (COM) 9: Rel 2 (NC)/Tacho 3"
- board text added: "4: Rel 5 (NO) 5: Rel 5 (COM) 6: Tacho 5 7: Rel 6 (NO) 8: Rel 6 (COM) 9: Tacho 6"
- board text added: "Battery safety controller V2.1 github.com/shining-man/bsc_fw created by T. Himmler 2022"
- board text added: "J2: 1=RX 2=TX 3=GND"
- board text added: "J4: Boot"
- board text removed: "1: Rel 1 (COM) 2: Rel 1 (NO) 3: Rel 1 (NC)/Tacho 1"
- board text removed: "1: Rel 4 (COM) 2: Rel 4 (NO) 3: Tacho 4"
- board text removed: "1=RX 2=TX 3=GND"
- board text removed: "4: Rel 2 (COM) 5: Rel 2 (NO) 6: Rel 2 (NC)/Tacho 2 7: Rel 3 (COM) 8: Rel 3 (NO) 9: Rel 2 (NC)/Tacho 3"
- board text removed: "4: Rel 5 (COM) 5: Rel 5 (NO) 6: Tacho 5 7: Rel 6 (COM) 8: Rel 6 (NO) 9: Tacho 6"
- board text removed: "Battery safety controller V2.0 github.com/shining-man/bsc_fw created by T. Himmler 2022"
- board text removed: "Boot"

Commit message: Change extension bus
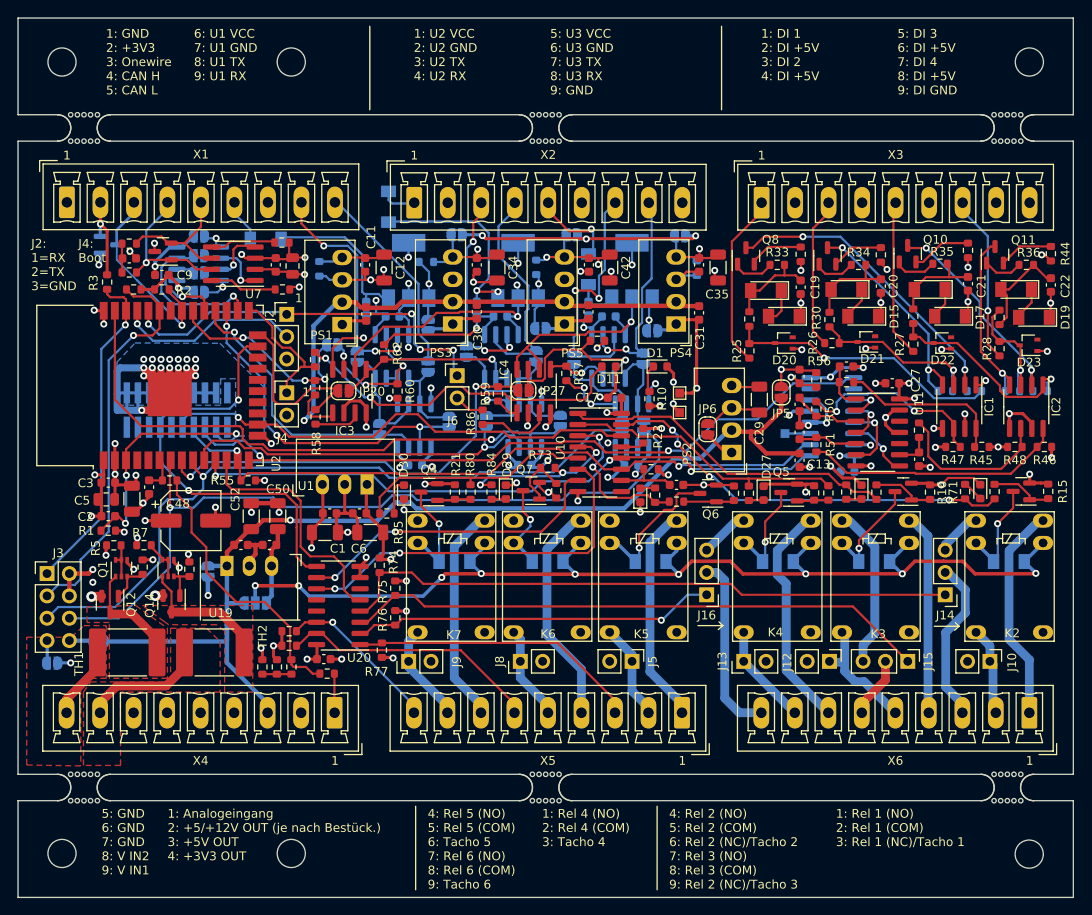
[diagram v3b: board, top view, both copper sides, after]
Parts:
- removed J11: Conn_Extension, Connector_PinHeader_2.54mm:PinHeader_2x03_P2.54mm_Vertical
- added D31: BAT54S, Package_TO_SOT_SMD:SOT-23, B.Cu at (40.3, 41.8)
- added H5: MountingHole, MountingHole:MountingHole_3.2mm_M3, F.Cu at (61.1, 111.0)
- added H6: MountingHole, MountingHole:MountingHole_3.2mm_M3, F.Cu at (145.0, 111.1)
- added J3: Conn_Extension, bsc_custom:PinHeader_2x04_P2.54mm_Vertical_jlc, F.Cu at (34.6, 83.0)
- added J6: JP_U3TX_EN, bsc_custom:PinHeader_1x02_P2.54mm_Vertical_jlc, F.Cu at (79.9, 57.9)
- added R86: 330R, Resistor_SMD:R_0603_1608Metric, F.Cu at (82.8, 61.4)
- added R87: 2k2, Resistor_SMD:R_0603_1608Metric, F.Cu at (92.4, 56.4)
- C4: footprint Capacitor_SMD:C_0805_2012Metric -> Capacitor_SMD:C_1206_3216Metric
- D20, D21, D22, D23: footprint Package_TO_SOT_SMD:SOT-23 -> Package_TO_SOT_SMD:SOT-323_SC-70
- IC1, IC2, IC3, IC4: footprint Package_SO:SOIC-8_5.23x5.23mm_P1.27mm -> Package_SO:SOIC-8_3.9x4.9mm_P1.27mm
- J10, J12, J13, J5, J8, J9: footprint Connector_PinHeader_2.54mm:PinHeader_1x02_P2.54mm_Vertical -> custom_th:PinHeader_1x02_P2.54mm_Vertical_jlc
- J14, J15, J16, J2: footprint Connector_PinHeader_2.54mm:PinHeader_1x03_P2.54mm_Vertical -> custom_th:PinHeader_1x03_P2.54mm_Vertical_jlc
- J4: footprint Connector_PinHeader_2.54mm:PinHeader_1x02_P2.54mm_Vertical -> bsc_custom:PinHeader_1x02_P2.54mm_Vertical_jlc
- JP13: moved to B.Cu
- PS2: value TEA 1-0505 -> 1S4E_0505S1U; footprint Converter_DCDC:Converter_DCDC_Murata_MEE1SxxxxSC_THT -> custom_th:Converter_DCDC_GAPTEC_1S4E_S1U
- R10, R24, R71, R81, R82, R83, R84, R85: value 270R -> 330R
- R19, R56, R63, R64, R65: value n.b. -> 330R
- moved H3 123.1 mm to (61.1, 21.0)
- moved X3 15.2 mm to (129.8, 37.0)
- moved X6 15.2 mm to (129.8, 95.0)
- moved X4 15.2 mm to (50.8, 95.0)
- moved X1 15.2 mm to (50.8, 37.0)
- moved X2 15.2 mm to (90.3, 37.0)
- moved X5 15.2 mm to (90.3, 95.0)
- moved JP28 9.25 mm to (51.6, 78.9)
- moved C6 5.16 mm to (70.1, 74.5), turned to 180 degrees
- moved C1 4.84 mm to (64.9, 74.5), turned to 0 degrees
- moved JP13 4.20 mm to (65.7, 53.2)
- moved C8 3.44 mm to (68.8, 72.3), turned to 180 degrees
- moved C7 3.39 mm to (65.4, 72.3), turned to 0 degrees
- moved C51 3.35 mm to (58.6, 75.9), turned to 180 degrees
- moved C53 3.20 mm to (55.3, 75.9), turned to 0 degrees
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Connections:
- IC4 pad 3: unconnected-(IC4-Pad3) -> Net-(IC4-Pad3)
- IC4 pad 4: unconnected-(IC4-Pad4) -> GND
- IC4 pad 5: unconnected-(IC4-Pad5) -> Net-(IC4-Pad5)
- IC4 pad 6: unconnected-(IC4-Pad6) -> /serial/U3_VCC
- U12 pad 4: +3V3 -> GND
- U12 pad 5: GND -> +3V3
- U9 pad 3: /serial/U3RXTX_ENs -> Net-(IC4-Pad5)
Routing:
- net GND: track 321.6 -> 383.0 mm, vias 55 -> 73
- net /U3TX: track 55.2 -> 84.1 mm
- net /U0RXD: track 18.9 -> 44.5 mm, vias 1 -> 4
- net /U3RX: track 71.4 -> 91.5 mm
- net /H_MISO: track 97.4 -> 82.8 mm
- net /RST_ESP: track 18.7 -> 29.4 mm
- net /H_CLK: track 87.9 -> 79.0 mm
- net Net-(IC4-Pad3): track 0.00 -> 8.56 mm
- net Net-(IC4-Pad5): track 0.00 -> 8.13 mm, vias 0 -> 1
- net +5V: track 183.5 -> 188.4 mm
- net V_IN: track 169.2 -> 164.6 mm
- net /serial/U3_VCC: track 38.1 -> 42.3 mm
- net /T_ADDR2: track 52.6 -> 48.5 mm
- net +3V3: track 167.8 -> 171.5 mm, vias 33 -> 32
- net /H_MOSI: track 58.3 -> 54.8 mm
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- added copper zone on B.Cu, net GND
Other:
- board text added: "1: Analogeingang 2: +5/+12V OUT (je nach Bestück.) 3: +5V OUT 4: +3V3 OUT"
- board text added: "Battery safety controller V2.3 github.com/shining-man/bsc_fw created by shiningman"
- board text removed: "1: Analogeingang 2: +5/+12V (je nach Bestückung) 3: +5V 4: +3V3"
- board text removed: "Battery safety controller V2.1 github.com/shining-man/bsc_fw created by T. Himmler 2022"
